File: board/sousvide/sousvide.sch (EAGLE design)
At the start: 15 parts, among them K1 G5L, Q1 BC548

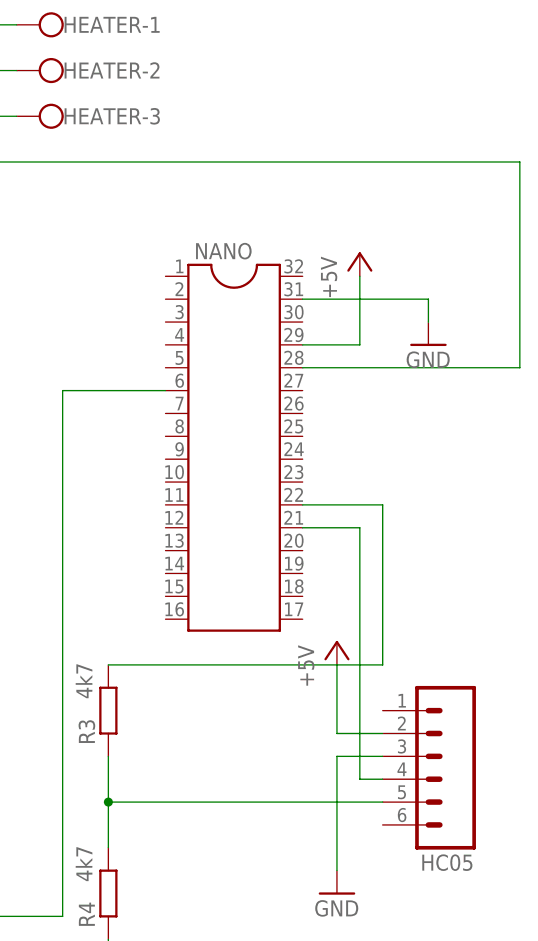
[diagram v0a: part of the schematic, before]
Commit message: Board change
Changed design so the BT module can fit over the board
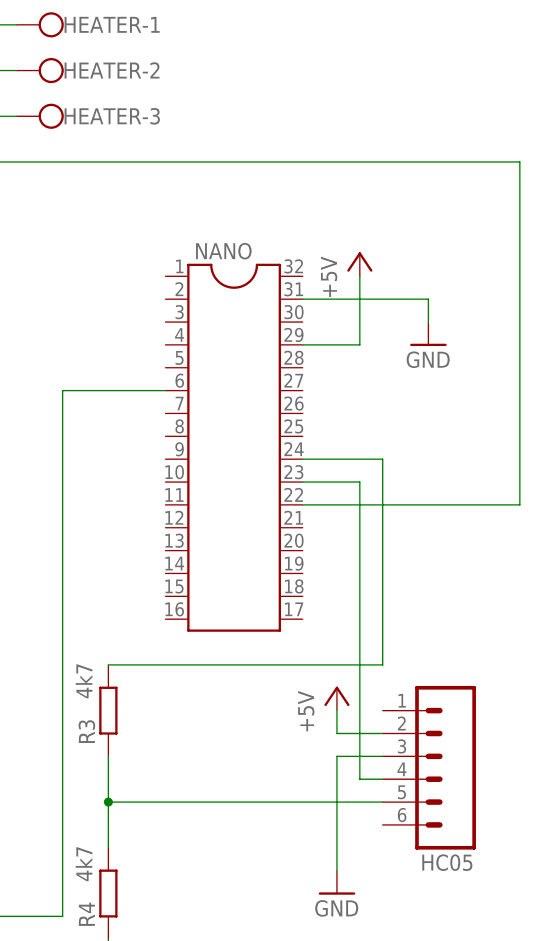
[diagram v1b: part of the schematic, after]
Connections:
- net N$10 renamed BTRX
- net N$11 renamed RELAYNC
- net N$3 renamed RELAYNA
- net N$5 renamed RELAYCONTROL
- removed net N$12: NANO.22, R3.2
- removed net N$4: DS18B20.2, NANO.28, R2.1
- removed net N$9: HC05.4, NANO.21
- new net NANORX: HC05.4, NANO.23
- new net NANOTX: NANO.24, R3.2
- new net ONEWIRE: DS18B20.2, NANO.22, R2.1
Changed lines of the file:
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@@
 <class number="0" name="default" width="0" drill="0">
+</class>
+<class number="1" name="power" width="3.81" drill="0">
 </class>
 </classes>
@@
 <attribute name="VALUE" x="76.2" y="-25.4" size="1.778" layer="96"/>
 </instance>
-<instance part="P+6" gate="1" x="78.74" y="5.08" smashed="yes">
-<attribute name="VALUE" x="76.2" y="0" size="1.778" layer="96" rot="R90"/>
+<instance part="P+6" gate="1" x="78.74" y="0" smashed="yes">
+<attribute name="VALUE" x="76.2" y="-5.08" size="1.778" layer="96" rot="R90"/>
 </instance>
 <instance part="F1" gate="1" x="38.1" y="81.28" smashed="yes" rot="R90">
@@
 <pinref part="P+6" gate="1" pin="+5V"/>
 <wire x1="83.82" y1="-5.08" x2="78.74" y2="-5.08" width="0.1524" layer="91"/>
-<wire x1="78.74" y1="-5.08" x2="78.74" y2="2.54" width="0.1524" layer="91"/>
+<wire x1="78.74" y1="-5.08" x2="78.74" y2="-2.54" width="0.1524" layer="91"/>
 </segment>
 </net>
@@
 </segment>
 </net>
-<net name="N$4" class="0">
+<net name="ONEWIRE" class="0">
 <segment>
 <pinref part="DS18B20" gate="G$1" pin="2"/>
@@
 <junction x="10.16" y="25.4"/>
 <wire x1="33.02" y1="58.42" x2="99.06" y2="58.42" width="0.1524" layer="91"/>
-<wire x1="99.06" y1="58.42" x2="99.06" y2="35.56" width="0.1524" layer="91"/>
-<pinref part="NANO" gate="G$1" pin="28"/>
-<wire x1="74.93" y1="35.56" x2="99.06" y2="35.56" width="0.1524" layer="91"/>
+<wire x1="99.06" y1="20.32" x2="99.06" y2="58.42" width="0.1524" layer="91"/>
+<pinref part="NANO" gate="G$1" pin="22"/>
+<wire x1="74.93" y1="20.32" x2="99.06" y2="20.32" width="0.1524" layer="91"/>
 </segment>
 </net>
@@
 </segment>
 </net>
-<net name="N$10" class="0">
+<net name="BTRX" class="0">
 <segment>
 <pinref part="R4" gate="G$1" pin="2"/>
@@
 </segment>
 </net>
-<net name="N$5" class="0">
+<net name="RELAYCONTROL" class="0">
 <segment>
 <pinref part="NANO" gate="G$1" pin="6"/>
@@
 </segment>
 </net>
-<net name="N$12" class="0">
-<segment>
-<pinref part="NANO" gate="G$1" pin="22"/>
-<wire x1="74.93" y1="20.32" x2="83.82" y2="20.32" width="0.1524" layer="91"/>
+<net name="NANOTX" class="0">
+<segment>
 <pinref part="R3" gate="G$1" pin="2"/>
 <wire x1="53.34" y1="2.54" x2="83.82" y2="2.54" width="0.1524" layer="91"/>
-<wire x1="83.82" y1="2.54" x2="83.82" y2="20.32" width="0.1524" layer="91"/>
-</segment>
-</net>
-<net name="N$9" class="0">
-<segment>
-<pinref part="NANO" gate="G$1" pin="21"/>
-<wire x1="74.93" y1="17.78" x2="81.28" y2="17.78" width="0.1524" layer="91"/>
+<wire x1="83.82" y1="2.54" x2="83.82" y2="25.4" width="0.1524" layer="91"/>
+<pinref part="NANO" gate="G$1" pin="24"/>
+<wire x1="74.93" y1="25.4" x2="83.82" y2="25.4" width="0.1524" layer="91"/>
+</segment>
+</net>
+<net name="NANORX" class="0">
+<segment>
 <pinref part="HC05" gate="G$1" pin="4"/>
 <wire x1="83.82" y1="-10.16" x2="81.28" y2="-10.16" width="0.1524" layer="91"/>
-<wire x1="81.28" y1="17.78" x2="81.28" y2="-10.16" width="0.1524" layer="91"/>
-</segment>
-</net>
-<net name="N$11" class="0">
+<wire x1="81.28" y1="22.86" x2="81.28" y2="-10.16" width="0.1524" layer="91"/>
+<pinref part="NANO" gate="G$1" pin="23"/>
+<wire x1="74.93" y1="22.86" x2="81.28" y2="22.86" width="0.1524" layer="91"/>
+</segment>
+</net>
+<net name="RELAYNC" class="1">
 <segment>
 <pinref part="K1" gate="2" pin="O"/>
@@
 </segment>
 </net>
-<net name="N$3" class="0">
+<net name="RELAYNA" class="1">
 <segment>
 <pinref part="HEATER" gate="-1" pin="KL"/>
@@
 </segment>
 </net>
-<net name="N$8" class="0">
+<net name="N$8" class="1">
 <segment>
 <pinref part="F1" gate="1" pin="1"/>

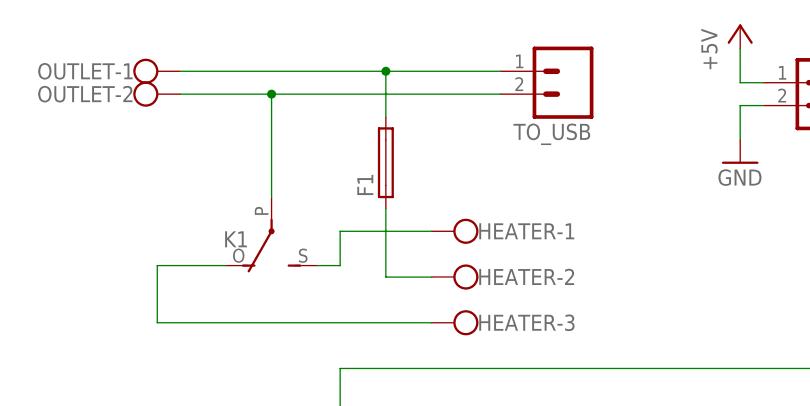
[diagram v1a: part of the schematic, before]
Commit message: New fuse
Updating fuse holder footprint to match the one we bought
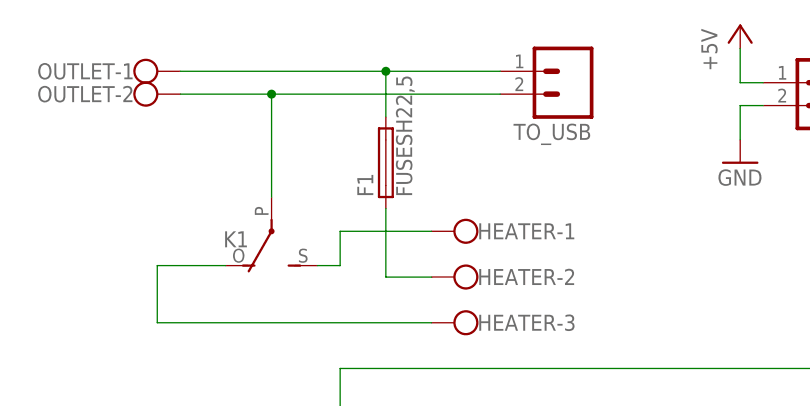
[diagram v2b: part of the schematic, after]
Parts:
- F1: value (none) -> FUSESH22,5; device fuse:SH25 -> fuse:FUSESH22,5
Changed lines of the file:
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@@
 <part name="GND6" library="supply1" library_urn="urn:adsk.eagle:library:371" deviceset="GND" device=""/>
 <part name="P+6" library="supply1" library_urn="urn:adsk.eagle:library:371" deviceset="+5V" device=""/>
-<part name="F1" library="fuse" library_urn="urn:adsk.eagle:library:233" deviceset="SH25" device="" package3d_urn="urn:adsk.eagle:package:14066/1"/>
 <part name="GND7" library="supply1" library_urn="urn:adsk.eagle:library:371" deviceset="GND" device=""/>
 <part name="HEATER" library="con-wago-500" library_urn="urn:adsk.eagle:library:195" deviceset="W237-103" device="" package3d_urn="urn:adsk.eagle:package:10691/1"/>
 <part name="OUTLET" library="con-wago-500" library_urn="urn:adsk.eagle:library:195" deviceset="W237-102" device="" package3d_urn="urn:adsk.eagle:package:10688/1"/>
+<part name="F1" library="fuse" library_urn="urn:adsk.eagle:library:233" deviceset="FUSE" device="SH22,5" package3d_urn="urn:adsk.eagle:package:14059/1"/>
 </parts>
 <sheets>
@@
 <attribute name="VALUE" x="76.2" y="-5.08" size="1.778" layer="96" rot="R90"/>
 </instance>
-<instance part="F1" gate="1" x="38.1" y="81.28" smashed="yes" rot="R90">
-<attribute name="NAME" x="36.703" y="77.47" size="1.778" layer="95" rot="R90"/>
-<attribute name="VALUE" x="41.021" y="77.47" size="1.778" layer="96" rot="R90"/>
-</instance>
 <instance part="GND7" gate="1" x="88.9" y="38.1" smashed="yes">
 <attribute name="VALUE" x="86.36" y="35.56" size="1.778" layer="96"/>
@@
 <attribute name="VALUE" x="7.62" y="85.217" size="1.778" layer="96"/>
 <attribute name="NAME" x="10.16" y="89.789" size="1.778" layer="95" rot="R180"/>
+</instance>
+<instance part="F1" gate="G$1" x="38.1" y="81.28" smashed="yes" rot="R90">
+<attribute name="NAME" x="36.703" y="77.47" size="1.778" layer="95" rot="R90"/>
+<attribute name="VALUE" x="41.021" y="77.47" size="1.778" layer="96" rot="R90"/>
 </instance>
 </instances>
@@
 <pinref part="TO_USB" gate="G$1" pin="1"/>
 <wire x1="15.24" y1="91.44" x2="38.1" y2="91.44" width="0.1524" layer="91"/>
-<pinref part="F1" gate="1" pin="2"/>
 <wire x1="38.1" y1="91.44" x2="50.8" y2="91.44" width="0.1524" layer="91"/>
 <wire x1="38.1" y1="86.36" x2="38.1" y2="91.44" width="0.1524" layer="91"/>
 <junction x="38.1" y="91.44"/>
 <pinref part="OUTLET" gate="-1" pin="KL"/>
+<pinref part="F1" gate="G$1" pin="2"/>
 </segment>
 </net>
@@
 <net name="N$8" class="1">
 <segment>
-<pinref part="F1" gate="1" pin="1"/>
 <wire x1="38.1" y1="76.2" x2="38.1" y2="68.58" width="0.1524" layer="91"/>
 <pinref part="HEATER" gate="-2" pin="KL"/>
 <wire x1="38.1" y1="68.58" x2="43.18" y2="68.58" width="0.1524" layer="91"/>
-</segment>
-</net>
+<pinref part="F1" gate="G$1" pin="1"/>
+</segment>
+</net>

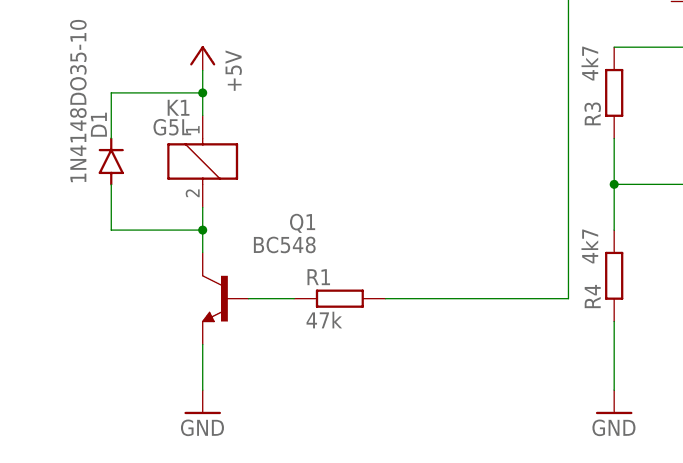
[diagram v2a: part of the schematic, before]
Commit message: Board corrections
Changed relay transistor to PNP, to avoid turning the heater on during reset and with the device turned off.
Changed transistor base resistor to 4k7. Old value did not allowed enough current to switch the relay.
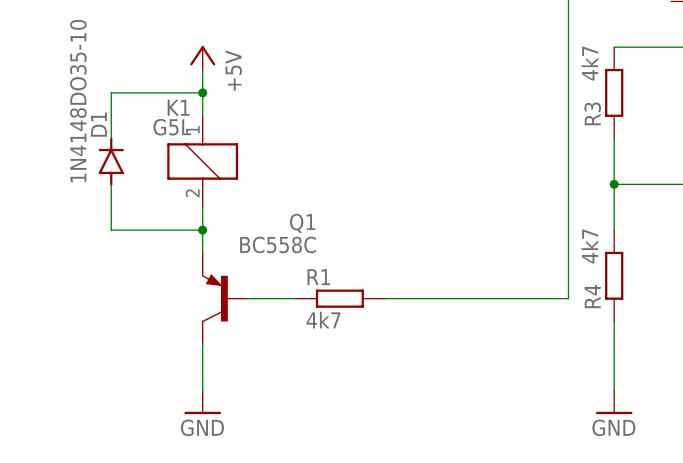
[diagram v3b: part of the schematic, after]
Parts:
- Q1: value BC548 -> BC558C; device transistor-npn:BC548 -> transistor-pnp:BC558C
- R1: value 47k -> 4k7
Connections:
- net GND: now also Q1.C; no longer Q1.E
- net N$6: now also Q1.E; no longer Q1.C
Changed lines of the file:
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@@
 <part name="NANO" library="ic-package" library_urn="urn:adsk.eagle:library:239" deviceset="DIL32" device="" package3d_urn="urn:adsk.eagle:package:18076/2"/>
 <part name="P+5" library="supply1" library_urn="urn:adsk.eagle:library:371" deviceset="+5V" device=""/>
-<part name="R1" library="rcl" library_urn="urn:adsk.eagle:library:334" deviceset="R-EU_" device="0204/7" package3d_urn="urn:adsk.eagle:package:23498/2" value="47k"/>
-<part name="Q1" library="transistor-npn" library_urn="urn:adsk.eagle:library:398" deviceset="BC548*" device="" package3d_urn="urn:adsk.eagle:package:28989/2"/>
+<part name="R1" library="rcl" library_urn="urn:adsk.eagle:library:334" deviceset="R-EU_" device="0204/7" package3d_urn="urn:adsk.eagle:package:23498/2" value="4k7"/>
+<part name="Q1" library="transistor-pnp" library_urn="urn:adsk.eagle:library:399" deviceset="BC558*" device="" package3d_urn="urn:adsk.eagle:package:29218/2" technology="C"/>
 <part name="D1" library="diode" library_urn="urn:adsk.eagle:library:210" deviceset="1N4148" device="DO35-10" package3d_urn="urn:adsk.eagle:package:43344/2" value="1N4148DO35-10"/>
 <part name="GND2" library="supply1" library_urn="urn:adsk.eagle:library:371" deviceset="GND" device=""/>
@@
 </segment>
 <segment>
-<pinref part="Q1" gate="G$1" pin="E"/>
+<pinref part="Q1" gate="G$1" pin="C"/>
 <pinref part="GND2" gate="1" pin="GND"/>
 <wire x1="7.62" y1="-35.56" x2="7.62" y2="-30.48" width="0.1524" layer="91"/>
@@
 <net name="N$6" class="0">
 <segment>
-<pinref part="Q1" gate="G$1" pin="C"/>
+<pinref part="Q1" gate="G$1" pin="E"/>
 <pinref part="K1" gate="1" pin="2"/>
 <wire x1="7.62" y1="-15.24" x2="7.62" y2="-17.78" width="0.1524" layer="91"/>

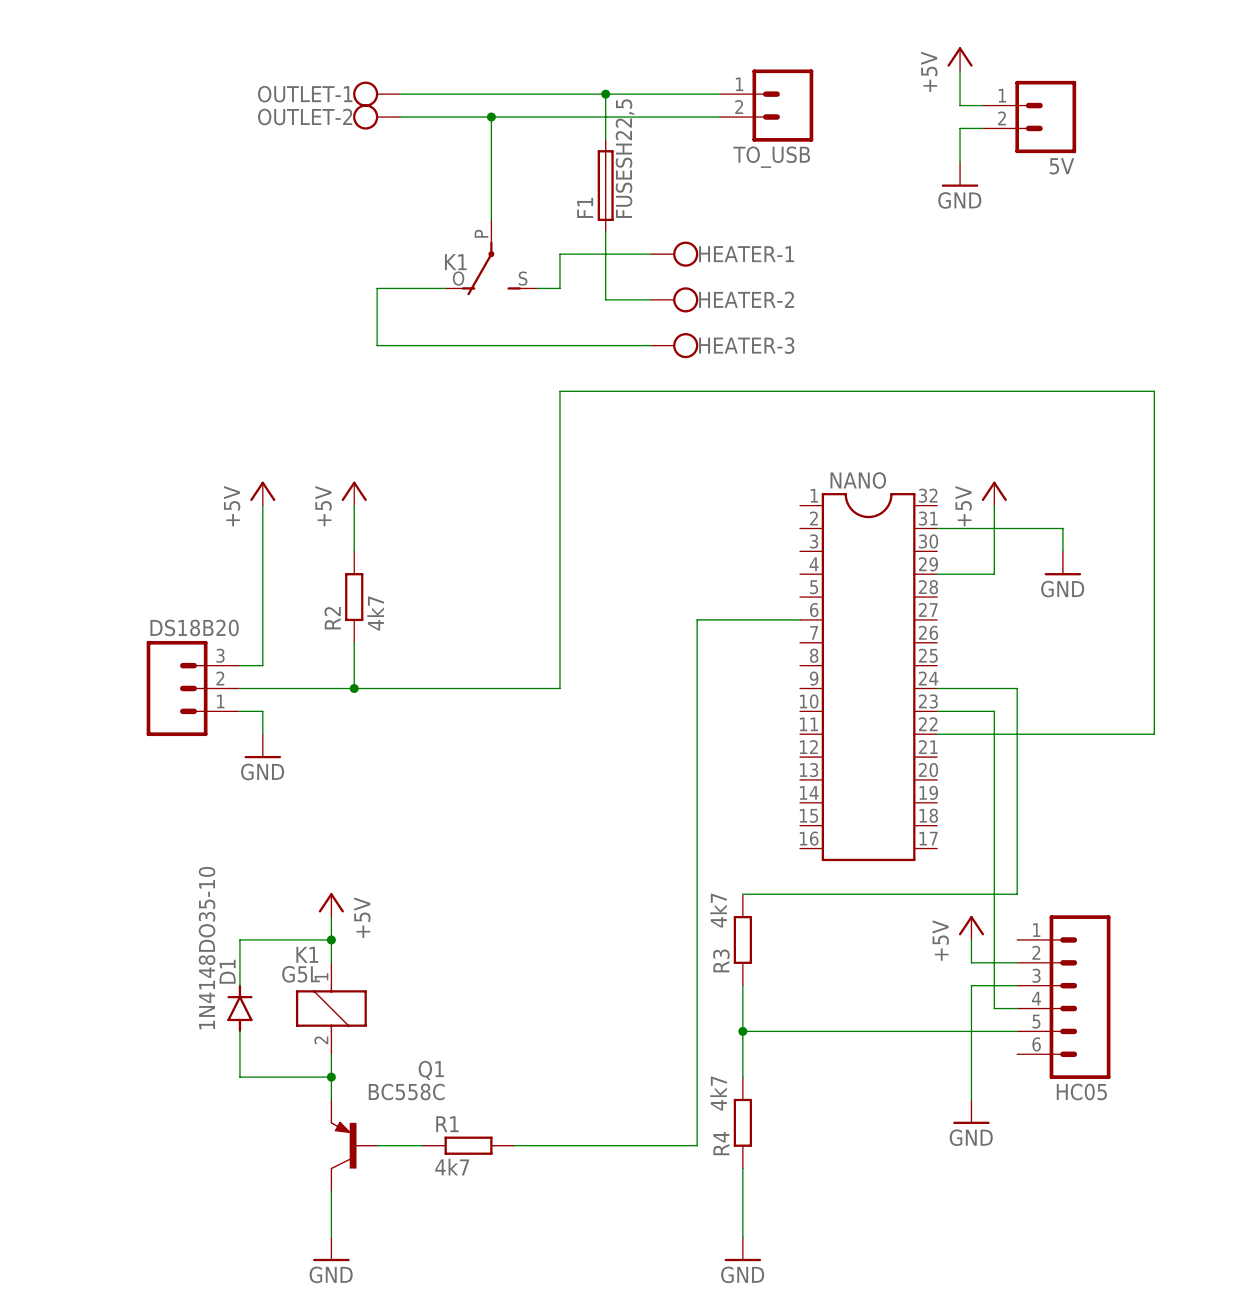
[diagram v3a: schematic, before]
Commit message: Connectors update
Changing connectors to better match physical ones. Created better labels in silk layer.
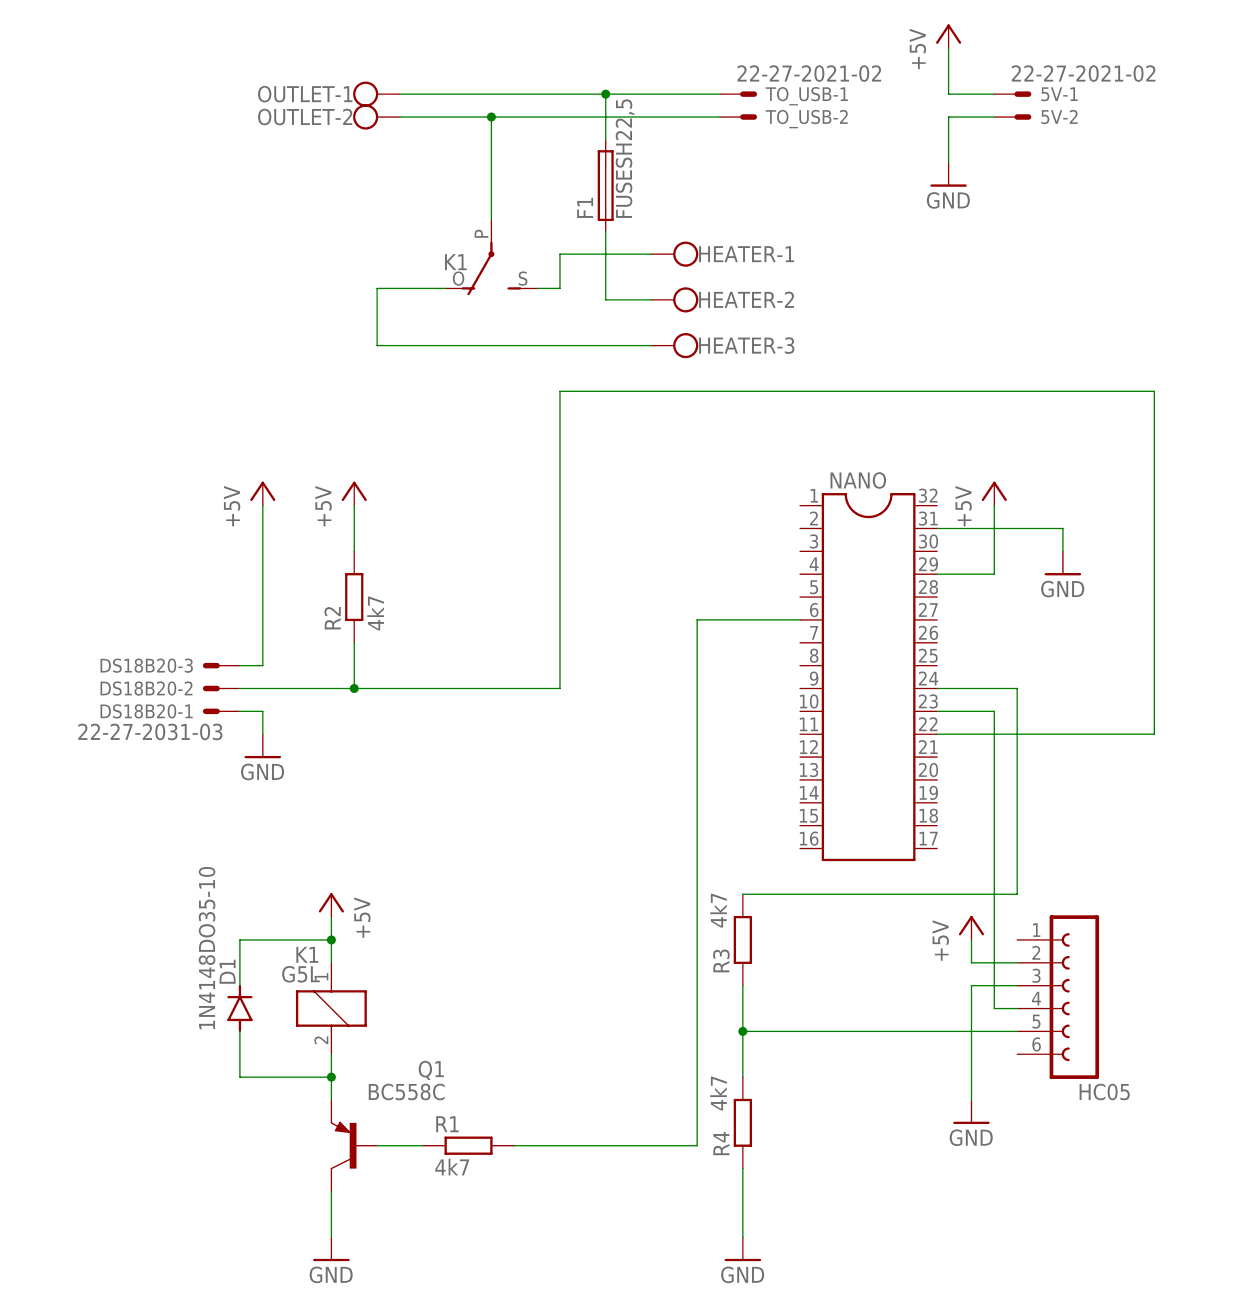
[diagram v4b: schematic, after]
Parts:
- 5V, TO_USB: value (none) -> 22-27-2021-02; device con-amp-quick:M02 -> con-molex:22-27-2021-02
- DS18B20: value (none) -> 22-27-2031-03; device con-amp-quick:M03 -> con-molex:22-27-2031-03
- HC05: device con-amp-quick:M06 -> con-lsta:FE06-1
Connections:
- net +5V: now also 5V-1.S, DS18B20-3.S; no longer 5V.1, DS18B20.3
- net GND: now also 5V-2.S, DS18B20-1.S; no longer 5V.2, DS18B20.1
- net N$1: now also TO_USB-1.S; no longer TO_USB.1
- net N$2: now also TO_USB-2.S; no longer TO_USB.2
- net ONEWIRE: now also DS18B20-2.S; no longer DS18B20.2
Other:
- moved on the sheet: HC05
